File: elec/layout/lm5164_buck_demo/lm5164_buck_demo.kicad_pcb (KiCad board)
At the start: 2 copper layers, 40 x 40 mm, 14 parts

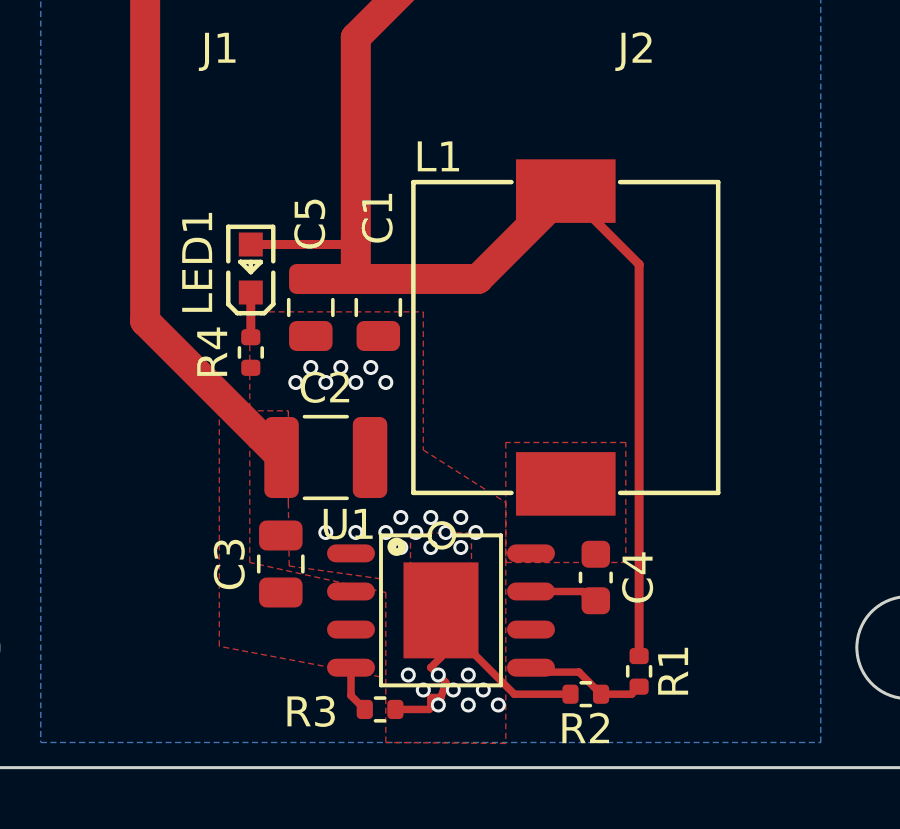
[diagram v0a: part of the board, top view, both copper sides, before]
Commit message: add to bikey-wagon.ato, add feedback ripple circuit
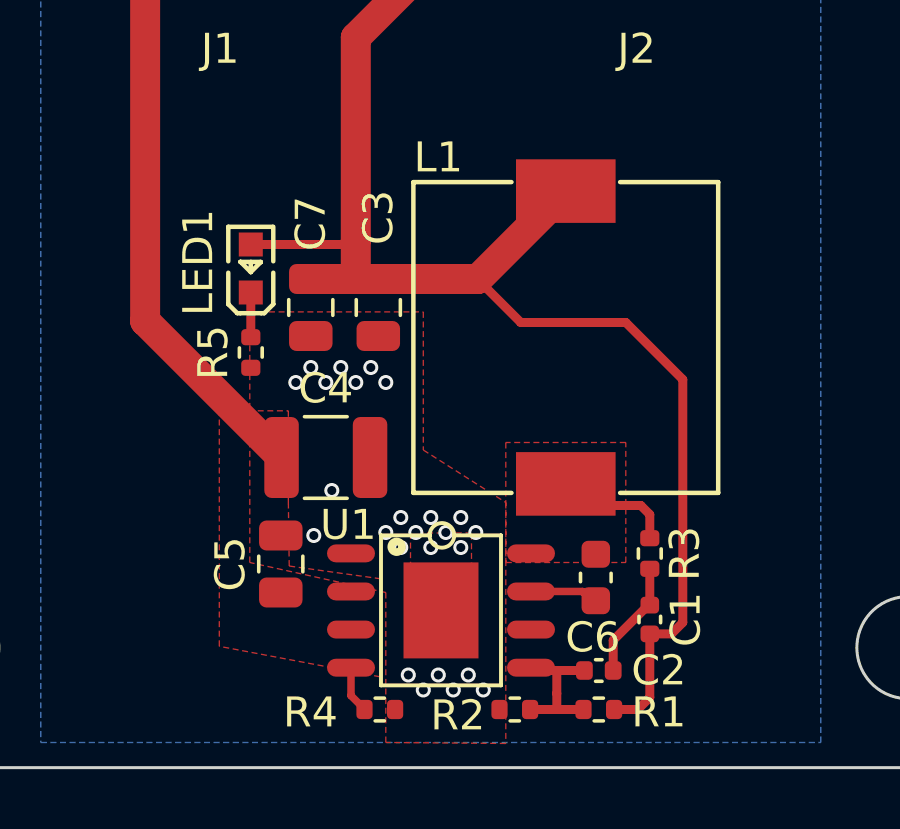
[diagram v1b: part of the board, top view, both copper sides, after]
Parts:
- added C1: 50V 4.7nF X7R ±10% 0402 Multilayer Ceramic Capacitors MLCC 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, lib:C0402, F.Cu at (155.8, 115.9)
- added C2: 50V 47pF C0G ±5% 0402 Multilayer Ceramic Capacitors MLCC - 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, lib:C0402, F.Cu at (154.1, 117.6)
- added R3: 62.5mW Thick Film Resistors 50V ±100ppm/℃ ±1% 374kΩ 0402 Ch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, lib:R0402, F.Cu at (155.8, 113.7)
- R1: value 62.5mW Thick Film Resistors 50V ±100ppm/℃ ±1% 66.5kΩ 0402 Chip Resistor - Surface Mount ROHS -> 62.5mW Thick Film Resistors 50V ±100ppm/℃ ±1% 374kΩ 0402 Chip Resistor - Surface Mount ROHS
- R2: value 62.5mW Thick Film Resistors 50V ±100ppm/℃ ±1% 9.1kΩ 0402 Chip Resistor - Surface Mount ROHS -> 62.5mW Thick Film Resistors 50V ±100ppm/℃ ±1% 51kΩ 0402 Chip Resistor - Surface Mount ROHS
- R4: renamed from R3; value 62.5mW Thick Film Resistors 50V ±100ppm/℃ ±1% 62kΩ 0402 Chip Resistor - Surface Mount ROHS -> 62.5mW Thick Film Resistors ±100ppm/℃ ±1% 69.8kΩ 0402 Chip Resistor - Surface Mount ROHS
- R5: renamed from R4; value 62.5mW Thick Film Resistors 50V ±100ppm/℃ ±1% 4.42kΩ 0402 Chip Resistor - Surface Mount ROHS -> 62.5mW Thick Film Resistors 50V ±100ppm/℃ ±1% 5.1kΩ 0402 Chip Resistor - Surface Mount ROHS
- moved R2 2.42 mm to (151.3, 118.9)
- moved R1 1.85 mm to (154.1, 118.9), turned to 180 degrees
- renumbered C1 to C3, C2 to C4, C3 to C5, C4 to C6, C5 to C7
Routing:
- net gnd: track 10.8 -> 0.00 mm, vias 28 -> 25
- net buck-vcc-1: track 46.4 -> 50.9 mm
- net sw: track 0.00 -> 4.01 mm
- net buck.Ra-vcc: track 0.00 -> 3.92 mm
- net out: track 4.07 -> 4.90 mm
